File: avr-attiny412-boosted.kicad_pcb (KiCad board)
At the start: 2 copper layers, 36 parts, among them J10 Conn_01x01, J11 Conn_01x01, J12 Conn_01x01, J13 Conn_01x01, J14 Conn_01x01, J15 Conn_01x01, J2 Conn_01x01, J3 Conn_01x01, J4 Conn_01x01, J5 Conn_01x01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

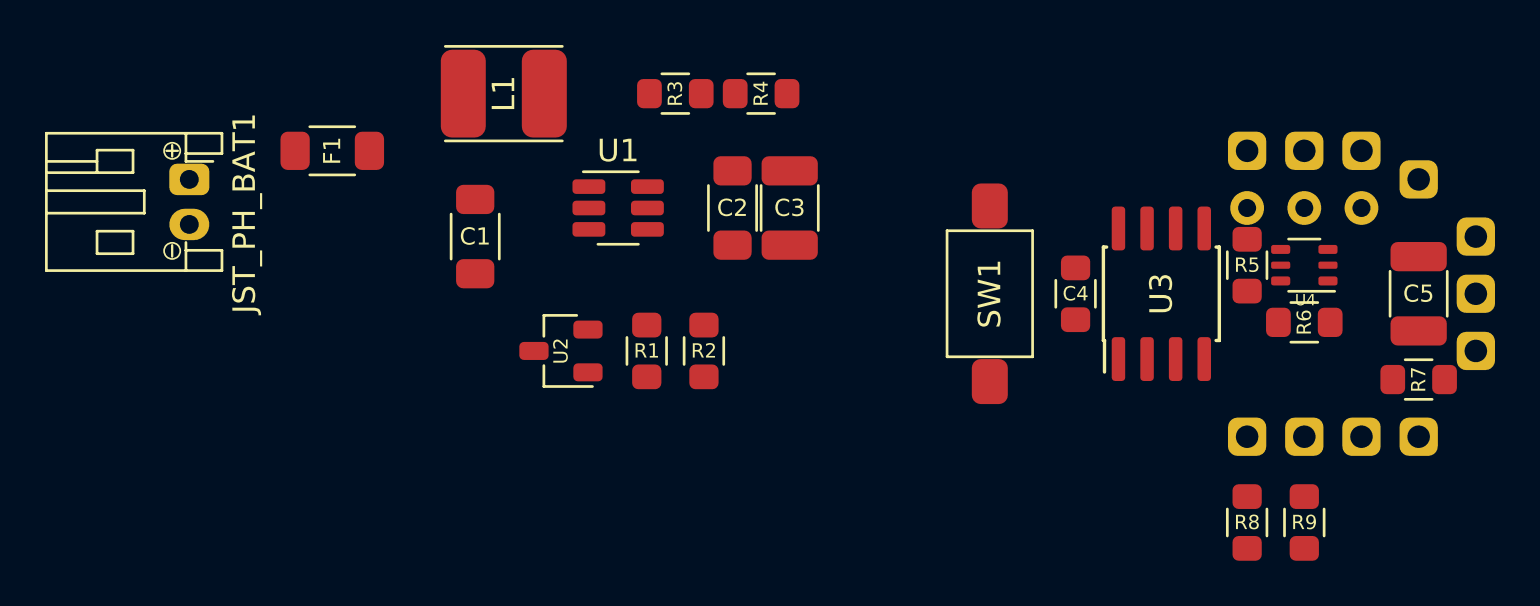
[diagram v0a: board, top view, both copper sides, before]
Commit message: Approximate placement, no routing
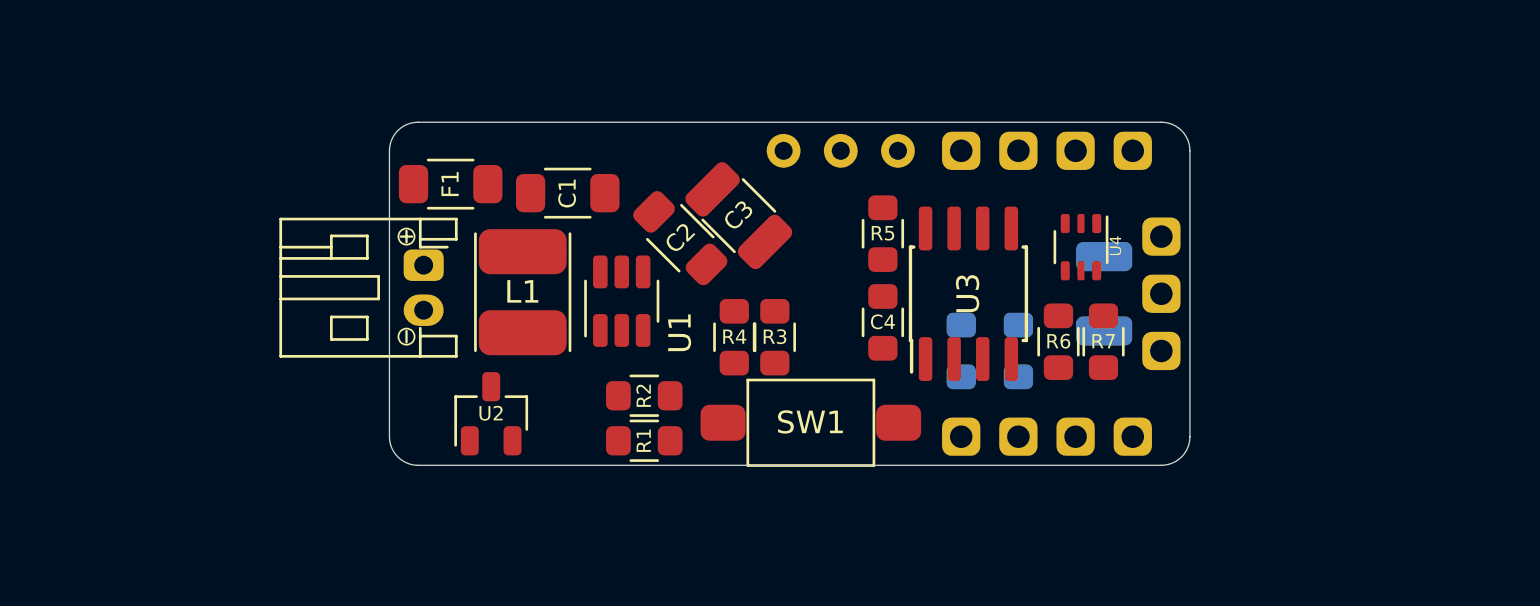
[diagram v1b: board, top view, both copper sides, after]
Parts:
- C5, R8, R9: moved to B.Cu
- moved J4 21.8 mm to (157.5, 96.5)
- moved J10 20.7 mm to (149.6, 96.5)
- moved J11 20.7 mm to (152.1, 96.5)
- moved J12 20.7 mm to (154.7, 96.5)
- moved J5 18.0 mm to (165.1, 96.5)
- moved J6 18.0 mm to (157.5, 109.2)
- moved J3 18.0 mm to (160.0, 96.5)
- moved J7 18.0 mm to (160.0, 109.2)
- moved J8 18.0 mm to (162.6, 109.2)
- moved J9 17.1 mm to (165.1, 109.2)
- moved R5 16.2 mm to (154.0, 100.2)
- moved R8 14.8 mm to (157.5, 105.4), turned to 270 degrees
- moved J2 14.8 mm to (162.6, 96.5)
- moved R9 14.8 mm to (160.0, 105.4), turned to 270 degrees
- moved R7 14.1 mm to (163.8, 105.0), turned to 270 degrees
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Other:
- board outline added: 35.6 x 15.2 mm

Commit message: Routed
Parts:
- moved R9 5.79 mm to (157.7, 100.1), turned to 90 degrees
- moved R8 5.68 mm to (159.5, 100.1), turned to 90 degrees
- moved R1 1.90 mm to (143.4, 107.5)
- moved R2 1.90 mm to (143.4, 109.3)
- moved C3 0.45 mm to (147.8, 99.8), turned to 305 degrees
- moved C2 0.28 mm to (145.2, 100.6), turned to 305 degrees
- moved C1 0.22 mm to (139.9, 98.6), turned to 0 degrees
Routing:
- net VPP: track 0.00 -> 41.1 mm, vias 0 -> 1
- net GND: track 0.00 -> 38.3 mm, vias 0 -> 19
- net VBAT: track 0.00 -> 28.3 mm
- net PA6: track 0.00 -> 14.9 mm, vias 0 -> 1
- net PA1: track 0.00 -> 14.5 mm, vias 0 -> 2
- net Net-(R5-Pad2): track 0.00 -> 13.3 mm, vias 0 -> 2
- net Net-(R1-Pad2): track 0.00 -> 11.5 mm
- net PA7: track 0.00 -> 9.83 mm
- net Net-(R3-Pad2): track 0.00 -> 8.55 mm
- net PA2: track 0.00 -> 7.00 mm
- net VSW: track 0.00 -> 6.77 mm
- net UPDI: track 0.00 -> 3.92 mm
- net Net-(F1-Pad2): track 0.00 -> 3.79 mm
- net Net-(L1-Pad2): track 0.00 -> 3.63 mm
- net PA3: track 0.00 -> 3.58 mm
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- added copper zone on B.Cu, net GND
- added copper zone on F.Cu, net Net-(L1-Pad2)
- added copper zone on F.Cu, net VPP

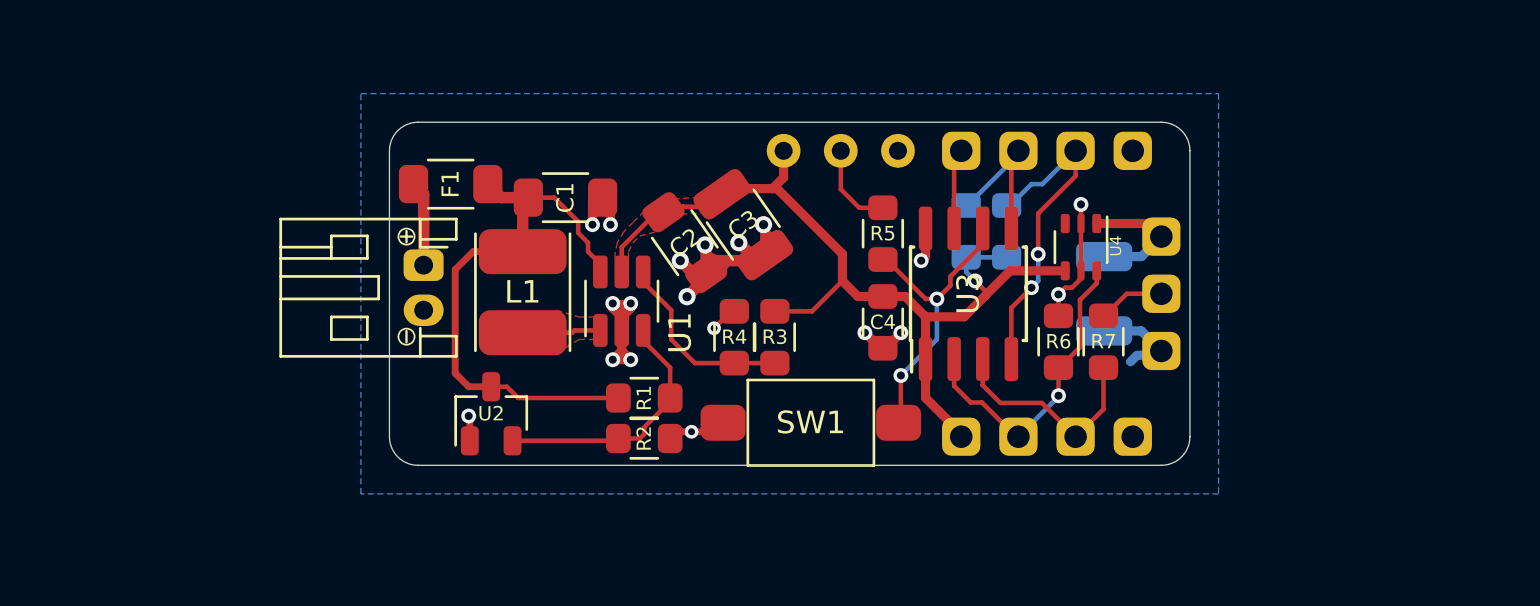
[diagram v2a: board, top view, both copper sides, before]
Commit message: Final layout and silkcreen. Add layout picture
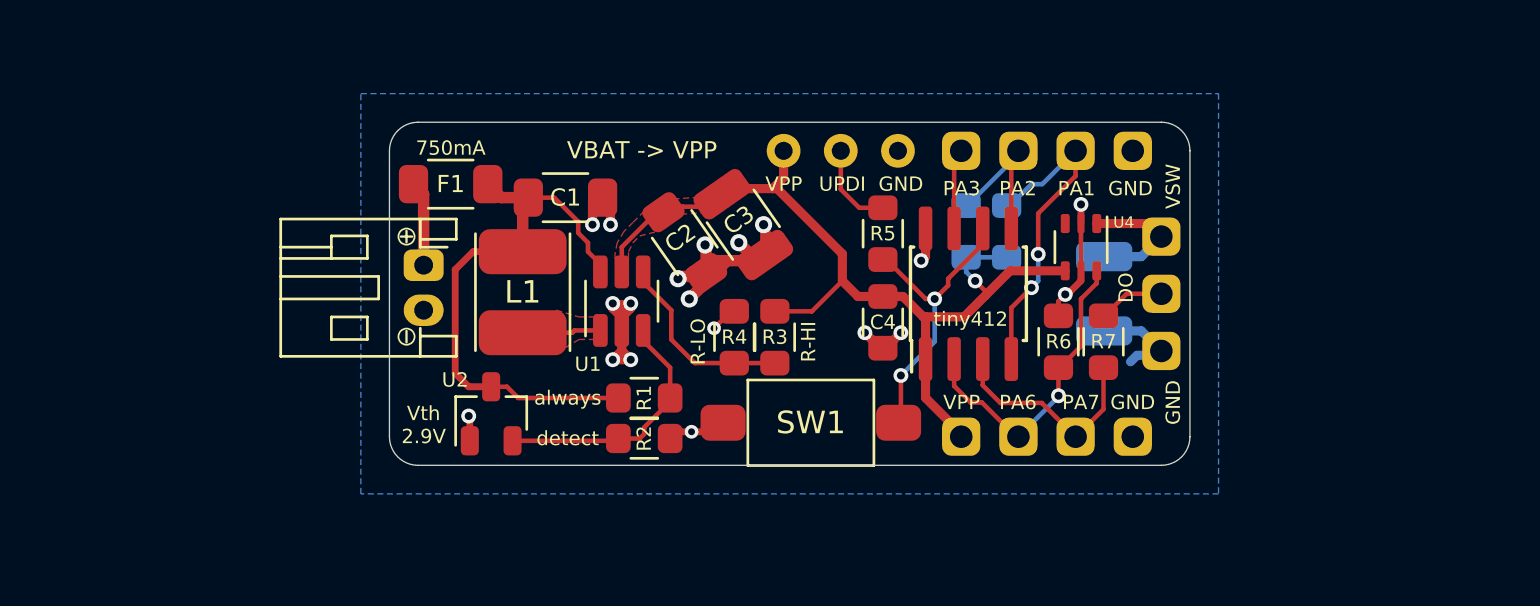
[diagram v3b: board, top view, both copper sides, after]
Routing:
- net GND: track 38.3 -> 38.9 mm
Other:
- board text added: "(C) Vlad Belous"
- board text added: "750mA"
- board text added: "AVR ATtiny412 with onboard boost reg MCP1640, MCP16251, or TPS6107x"
- board text added: "CC BY-SA 4.0"
- board text added: "DO"
- board text added: "GND"
- board text added: "I2C pull-ups"
- board text added: "PA1"
- board text added: "PA2"
- board text added: "PA3"
- board text added: "PA6"
- board text added: "PA7"
- board text added: "R-HI"
- board text added: "R-LO"
- board text added: "UPDI"
- board text added: "VBAT"
- board text added: "VBAT -> VPP"
- board text added: "VPP"
- board text added: "VSW"
- board text added: "Vth 2.9V"
- board text added: "always"
- board text added: "detect"
- board text added: "tiny412"

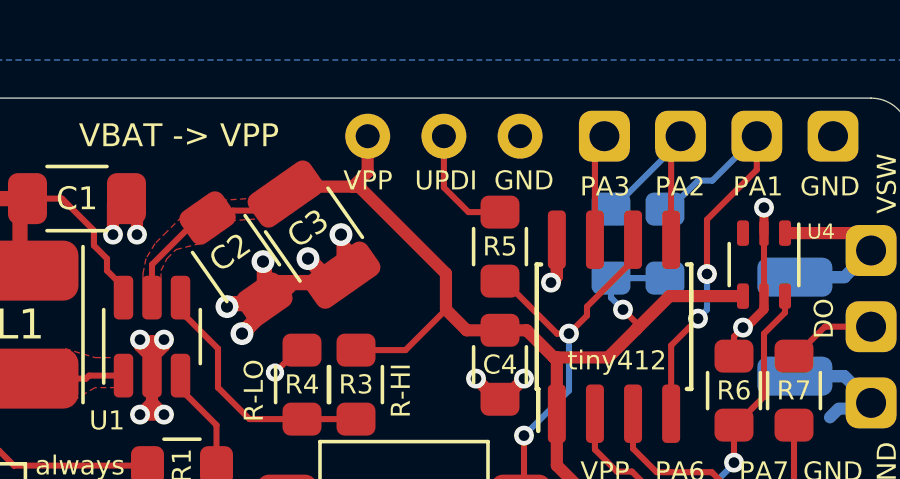
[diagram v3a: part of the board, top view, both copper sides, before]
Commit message: Adjust prog pin locations
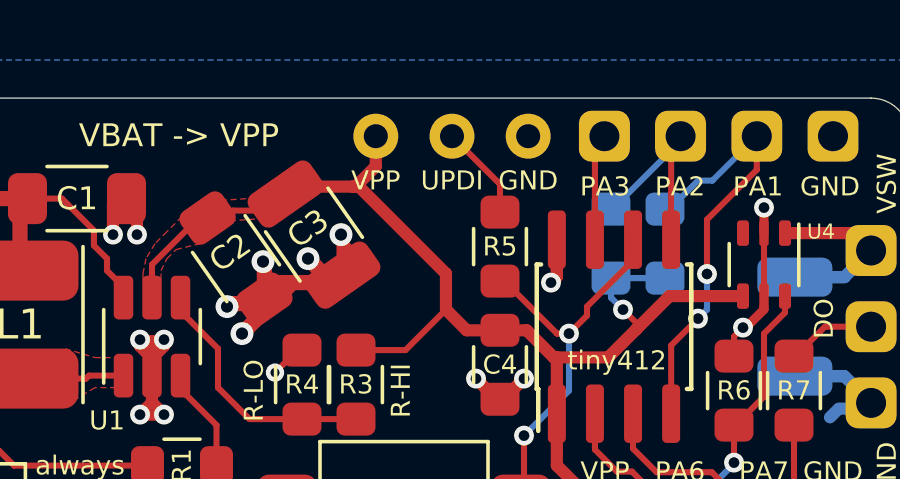
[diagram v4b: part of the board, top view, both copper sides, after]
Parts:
- moved J10 0.27 mm to (149.9, 96.5)
- moved J11 0.27 mm to (152.4, 96.5)
- moved J12 0.27 mm to (154.9, 96.5)
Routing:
- net UPDI: track 3.92 -> 3.19 mm
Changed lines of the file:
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@@
     (thickness 1.6)
     (drawings 40)
-    (tracks 230)
+    (tracks 231)
     (zones 0)
     (modules 36)
@@
   )
   (setup
-    (last_trace_width 0.508)
+    (last_trace_width 0.2032)
     (user_trace_width 0.3048)
     (user_trace_width 0.4064)
@@
   )
   (module local_footprints:Conn_1-wire (layer F.Cu)
-    (at 149.59 96.52 90)
+    (at 149.86 96.52 90)
     (descr "Through hole straight pin header, 1x07, 2.54mm pitch, single row")
     (tags "Through hole pin header THT 1x07 2.54mm single row")
@@
   )
   (module local_footprints:Conn_1-wire (layer F.Cu)
-    (at 152.13 96.52 90)
+    (at 152.4 96.52 90)
     (descr "Through hole straight pin header, 1x07, 2.54mm pitch, single row")
     (tags "Through hole pin header THT 1x07 2.54mm single row")
@@
   )
   (module local_footprints:Conn_1-wire (layer F.Cu)
-    (at 154.67 96.52 90)
+    (at 154.94 96.52 90)
     (descr "Through hole straight pin header, 1x07, 2.54mm pitch, single row")
     (tags "Through hole pin header THT 1x07 2.54mm single row")
@@
     (effects (font (size 0.635 0.635) (thickness 0.127)))
   )
-  (gr_text GND (at 154.8 98) (layer F.SilkS)
+  (gr_text GND (at 154.94 98) (layer F.SilkS)
     (effects (font (size 0.635 0.635) (thickness 0.127)))
   )
-  (gr_text UPDI (at 152.2 98) (layer F.SilkS)
+  (gr_text UPDI (at 152.4 98) (layer F.SilkS)
     (effects (font (size 0.635 0.635) (thickness 0.127)))
   )
-  (gr_text VPP (at 149.6 98) (layer F.SilkS)
+  (gr_text VPP (at 149.86 98) (layer F.SilkS)
     (effects (font (size 0.635 0.635) (thickness 0.127)))
   )
@@
   (segment (start 146.301998 99) (end 146.853599 98.448399) (width 0.2032) (layer F.Cu) (net 3))
   (segment (start 145.1 99) (end 146.301998 99) (width 0.2032) (layer F.Cu) (net 3))
-  (segment (start 149.59 97.71) (end 149.59 96.52) (width 0.4064) (layer F.Cu) (net 3))
   (segment (start 147.101998 98.2) (end 149.1 98.2) (width 0.4064) (layer F.Cu) (net 3))
-  (segment (start 149.1 98.2) (end 149.59 97.71) (width 0.4064) (layer F.Cu) (net 3))
   (segment (start 146.853599 98.448399) (end 147.101998 98.2) (width 0.4064) (layer F.Cu) (net 3))
   (segment (start 149.1 98.2) (end 149.3 98.2) (width 0.4064) (layer F.Cu) (net 3))
@@
   (segment (start 155.795 103.895) (end 154.89 102.99) (width 0.4064) (layer F.Cu) (net 3))
   (segment (start 155.895 103.895) (end 155.795 103.895) (width 0.4064) (layer F.Cu) (net 3))
+  (segment (start 149.86 96.79) (end 149.59 96.52) (width 0.4064) (layer F.Cu) (net 3))
+  (segment (start 149.86 97.525989) (end 149.86 96.79) (width 0.4064) (layer F.Cu) (net 3))
+  (segment (start 149.185989 98.2) (end 149.86 97.525989) (width 0.4064) (layer F.Cu) (net 3))
+  (segment (start 149.1 98.2) (end 149.185989 98.2) (width 0.4064) (layer F.Cu) (net 3))
   (segment (start 165.79 99.75) (end 166.37 100.33) (width 0.4064) (layer F.Cu) (net 4))
   (segment (start 163.5 99.75) (end 165.79 99.75) (width 0.4064) (layer F.Cu) (net 4))
@@
   (segment (start 158.435 106.935) (end 159.220303 107.720303) (width 0.2032) (layer F.Cu) (net 10))
   (segment (start 158.435 105.77) (end 158.435 106.935) (width 0.2032) (layer F.Cu) (net 10))
-  (segment (start 154 99.05) (end 152.95 99.05) (width 0.2032) (layer F.Cu) (net 11))
-  (segment (start 152.13 98.23) (end 152.13 96.52) (width 0.2032) (layer F.Cu) (net 11))
-  (segment (start 152.95 99.05) (end 152.13 98.23) (width 0.2032) (layer F.Cu) (net 11))
+  (segment (start 154 98.12) (end 152.4 96.52) (width 0.2032) (layer F.Cu) (net 11))
+  (segment (start 154 99.05) (end 154 98.12) (width 0.2032) (layer F.Cu) (net 11))
   (segment (start 163.8 103.85) (end 163.85 103.85) (width 0.2032) (layer F.Cu) (net 12))
   (segment (start 164.83 102.87) (end 166.37 102.87) (width 0.2032) (layer F.Cu) (net 12))
@@
     (min_thickness 0.0254)
     (keepout (tracks allowed) (vias allowed) (copperpour not_allowed))
-    (fill (arc_segments 32) (thermal_gap 0.0254) (thermal_bridge_width 0.0508) (smoothing chamfer) (radius 0.0508))
+    (fill (arc_segments 32) (thermal_gap 0.0254) (thermal_bridge_width 0.0508))
     (polygon
       (pts

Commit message: Clearance update
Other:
- rule pad_to_mask_clearance: 0 -> 0.0254
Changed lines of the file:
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@@
     (pad_size 1.524 1.524)
     (pad_drill 0.762)
-    (pad_to_mask_clearance 0)
+    (pad_to_mask_clearance 0.0254)
     (aux_axis_origin 0 0)
     (visible_elements FFFFFF7F)
     (pcbplotparams
       (layerselection 0x010f0_ffffffff)
-      (usegerberextensions false)
+      (usegerberextensions true)
       (usegerberattributes false)
       (usegerberadvancedattributes false)
       (creategerberjobfile false)
       (excludeedgelayer true)
-      (linewidth 0.076200)
+      (linewidth 0.025400)
       (plotframeref false)
       (viasonmask false)
@@
       (padsonsilk false)
       (subtractmaskfromsilk false)
-      (outputformat 4)
+      (outputformat 1)
       (mirror false)
       (drillshape 0)
       (scaleselection 1)
-      (outputdirectory "plot"))
+      (outputdirectory "plot2"))
   )
   (net 0 "")
